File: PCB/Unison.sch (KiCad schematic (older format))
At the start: 262 parts, among them J1 USB4085-GF-A_REVA, J2 Conn_02x05_Odd_Even, J3 Conn_01x03, U1 ATmega32U4-AU, Y1 16MHz

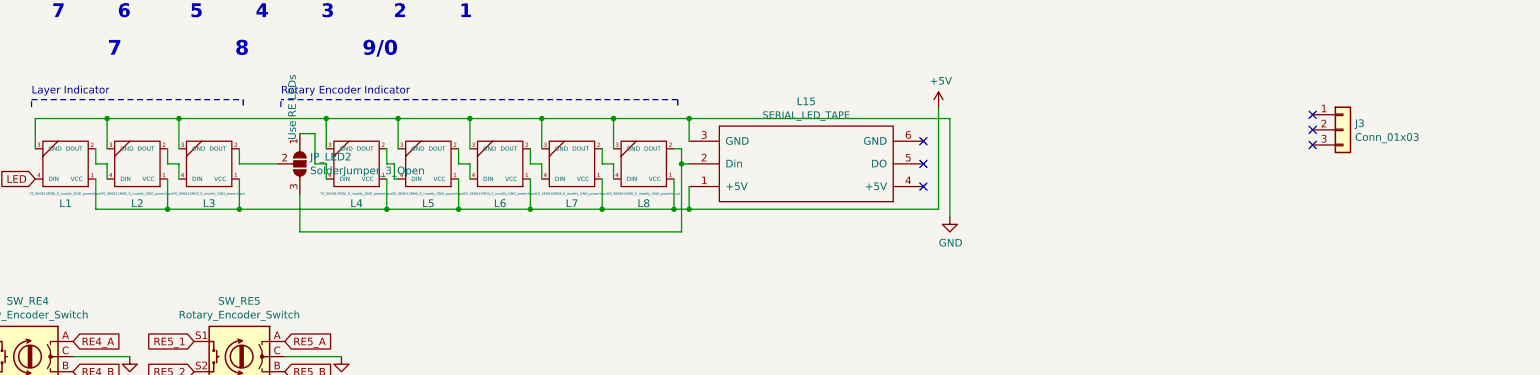
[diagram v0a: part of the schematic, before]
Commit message: OP-1スタイルで、4キー部分とミッドとトッププレートの間隔広げるに伴い、設置場所が狭くなるため、インジケータLEDを3個から2個に減らした。
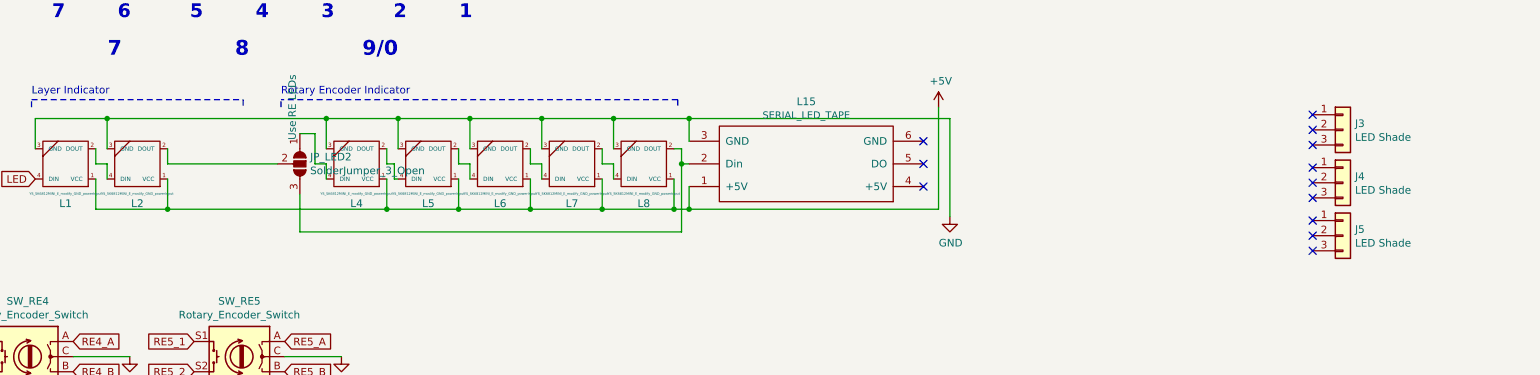
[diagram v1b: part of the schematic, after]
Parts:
- removed L3: YS_SK6812MINI_E_modify_GND_powerInput, mx2u:YS-SK6812MINI-E, symbol mx2u:YS_SK6812MINI_E_modify_GND_powerInput
- added J4, J5: LED Shade, Connector_PinSocket_2.54mm:PinSocket_1x03_P2.54mm_Vertical, symbol Connector_Generic:Conn_01x03
- J3: value Conn_01x03 -> LED Shade
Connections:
- net at JP_LED2.2 (C): now also L2.2 (DOUT)
- no-connect marks 9 -> 15
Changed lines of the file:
@@
 	6475 9525 6475 9625
-Wire Wire Line
-	6475 9625 6550 9625
-Wire Wire Line
-	6550 9625 6550 9725
-Wire Wire Line
-	6950 9525 6950 9625
 Wire Wire Line
 	7525 9625 7525 9725
@@
 	6475 9725 6475 9925
 Connection ~ 6475 9925
-Wire Wire Line
-	6475 9925 6950 9925
-Wire Wire Line
-	6950 9725 6950 9925
 Wire Wire Line
 	8400 9725 8400 9925
@@
 F 3 "" H 6275 9625 60  0001 C CNN
 	1    6275 9625
-	-1   0    0    1
-$EndComp
-$Comp
-L mx2u:YS_SK6812MINI_E_modify_GND_powerInput L3
-U 1 1 63211639
-P 6750 9625
-F 0 "L3" H 6750 9887 51  0000 C CNN
-F 1 "YS_SK6812MINI_E_modify_GND_powerInput" H 6750 9822 16  0000 C CNN
-F 2 "mx2u:YS-SK6812MINI-E" H 6750 9625 60  0001 C CNN
-F 3 "" H 6750 9625 60  0001 C CNN
-	1    6750 9625
 	-1   0    0    1
 $EndComp
@@
 Wire Wire Line
 	9425 9625 9425 9725
-Connection ~ 6950 9925
-Wire Wire Line
-	6950 9925 7925 9925
-Wire Wire Line
-	6950 9625 7200 9625
 Wire Wire Line
 	7350 9825 7350 10075
@@
 Wire Wire Line
 	6075 9325 5600 9325
-Wire Wire Line
-	6075 9325 6550 9325
 Connection ~ 6075 9325
 Wire Wire Line
 	6075 9525 6075 9325
-Wire Wire Line
-	6550 9525 6550 9325
-Wire Wire Line
-	6550 9325 7525 9325
-Connection ~ 6550 9325
 Connection ~ 7525 9325
 Wire Wire Line
@@
 P 14250 9400
 F 0 "J3" H 14330 9442 50  0000 L CNN
-F 1 "Conn_01x03" H 14330 9351 50  0000 L CNN
+F 1 "LED Shade" H 14330 9351 50  0000 L CNN
 F 2 "Connector_PinSocket_2.54mm:PinSocket_1x03_P2.54mm_Vertical" H 14250 9400 50  0001 C CNN
 F 3 "~" H 14250 9400 50  0001 C CNN
@@
 NoConn ~ 14050 9400
 NoConn ~ 14050 9500
+$Comp
+L Connector_Generic:Conn_01x03 J4
+U 1 1 60F74693
+P 14250 9750
+F 0 "J4" H 14330 9792 50  0000 L CNN
+F 1 "LED Shade" H 14330 9701 50  0000 L CNN
+F 2 "Connector_PinSocket_2.54mm:PinSocket_1x03_P2.54mm_Vertical" H 14250 9750 50  0001 C CNN
+F 3 "~" H 14250 9750 50  0001 C CNN
+	1    14250 9750
+	1    0    0    -1
+$EndComp
+NoConn ~ 14050 9650
+NoConn ~ 14050 9750
+NoConn ~ 14050 9850
+NoConn ~ 14050 10000
+NoConn ~ 14050 10100
+NoConn ~ 14050 10200
+$Comp
+L Connector_Generic:Conn_01x03 J5
+U 1 1 60FCE0DF
+P 14250 10100
+F 0 "J5" H 14330 10142 50  0000 L CNN
+F 1 "LED Shade" H 14330 10051 50  0000 L CNN
+F 2 "Connector_PinSocket_2.54mm:PinSocket_1x03_P2.54mm_Vertical" H 14250 10100 50  0001 C CNN
+F 3 "~" H 14250 10100 50  0001 C CNN
+	1    14250 10100
+	1    0    0    -1
+$EndComp
+Wire Wire Line
+	6075 9325 7525 9325
+Wire Wire Line
+	6475 9625 7200 9625
+Wire Wire Line
+	6475 9925 7925 9925
 $EndSCHEMATC

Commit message: Update: AU版、ひととおり完成。
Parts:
- removed J4, J5: LED Shade, Connector_PinSocket_2.54mm:PinSocket_1x03_P2.54mm_Vertical, symbol Connector_Generic:Conn_01x03
- removed L1, L2, L4, L5, L6, L7, L8: YS_SK6812MINI_E_modify_GND_powerInput, mx2u:YS-SK6812MINI-E, symbol mx2u:YS_SK6812MINI_E_modify_GND_powerInput
- added H1, H10, H11, H12, H13, H14, H15, H16, H17, H18, H2, H3, H4, H5, H6, H7, H8, H9: MountingHole, ukiha:M2_Hole, symbol Mechanical:MountingHole
- added J4: Conn_01x02, Connector_PinHeader_2.54mm:PinHeader_1x02_P2.54mm_Vertical, symbol Connector_Generic:Conn_01x02
- added JP_LED1: SolderJumper_3_Open, Jumper:SolderJumper-3_P1.3mm_Open_Pad1.0x1.5mm_NumberLabels, symbol Jumper:SolderJumper_3_Open
- added L1, L2, L3, L4, L5, L6, L7, L8, L9: SK6812MINI, LED_SMD:LED_SK6812MINI_PLCC4_3.5x3.5mm_P1.75mm, symbol swanmatch:SK6812MINI
- J2: value Conn_02x05_Odd_Even -> Conn_02x05[3_Odd_Even; footprint Connector_PinHeader_2.54mm:PinHeader_2x05_P2.54mm_Vertical -> Connector_PinHeader_2.54mm:PinHeader_2x03_P2.54mm_Vertical; symbol Connector_Generic:Conn_02x05_Odd_Even -> Connector_Generic:Conn_02x03_Odd_Even
- JP_LED2: Note Use RE LEDs -> RE LEDs
- SW_10_1, SW_12_1, SW_12_2, SW_13_1, SW_13_2, SW_14, SW_15, SW_16, SW_17_1, SW_19_1, SW_20_1, SW_23_1, SW_23_2, SW_24_1, SW_25_1, SW_26, SW_27_1, SW_27_2, SW_28_1, SW_28_2, SW_29, SW_30_1, SW_31, SW_32_1, SW_32_2, SW_34, SW_36_1, SW_36_2, SW_37_1, SW_38_1, SW_39_1, SW_40_1, SW_41_1, SW_41_2, SW_42, SW_43, SW_46_1, SW_46_2, SW_47, SW_48, SW_49, SW_50, SW_51_1, SW_51_2, SW_52, SW_54, SW_56, SW_57, SW_58, SW_59, SW_6, SW_60_1, SW_61, SW_62, SW_63, SW_64, SW_67, SW_68, SW_69, SW_70_1, SW_71, SW_72_1, SW_73_1, SW_74, SW_76, SW_78_1, SW_78_2, SW_79, SW_7_1, SW_80_1, SW_81, SW_82_1, SW_82_2, SW_83_1, SW_83_2, SW_84, SW_85_1, SW_86, SW_87_1, SW_87_2, SW_89, SW_9, SW_90_1, SW_94, SW_95, SW_96, SW_97_1, SW_97_2, SW_98_1, SW_98_2: footprint ukiha:CherryMX_MidHeight_16mm_rev2 -> ukiha:CherryMX_MidHeight_16mm_rev2_merged_hole
- SW_10_2, SW_19_2, SW_35_1, SW_35_2, SW_39_2, SW_45_1, SW_45_2, SW_65_1, SW_75_3, SW_85_2: footprint ukiha:CherryMX_MidHeight_16mm_rev2_2u_guide -> ukiha:CherryMX_MidHeight_16mm_rev2_merged_hole_2u_guide
- SW_17_2, SW_18_2, SW_20_2, SW_25_3, SW_30_2, SW_35_3, SW_38_2, SW_45_3, SW_45_4, SW_65_2, SW_65_3, SW_70_2, SW_72_2, SW_73_2, SW_7_2, SW_80_2, SW_85_3, SW_8_2: footprint ukiha:CherryMX_MidHeight_16mm_rev2_1.5u_guide -> ukiha:CherryMX_MidHeight_16mm_rev2_merged_hole_1.5u_guide
- SW_25_2, SW_60_2, SW_90_2: footprint ukiha:CherryMX_MidHeight_16mm_rev2_2U_vertical_guide -> ukiha:CherryMX_MidHeight_16mm_rev2_merged_hole_2U_vertical_guide
- SW_37_2: footprint ukiha:CherryMX_MidHeight_16mm_rev2_1.5u_alt_guide -> ukiha:CherryMX_MidHeight_16mm_rev2_merged_hole_1.5u_alt_guide
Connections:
- net +5V: now also L1.4 (VDD), L2.4 (VDD), L3.4 (VDD), L4.4 (VDD), L5.4 (VDD), L6.4 (VDD), L7.4 (VDD), L8.4 (VDD), L9.4 (VDD)
- net AUDIO: no longer J2.9 (Pin_9)
- net GND: now also L1.2 (VSS), L2.2 (VSS), L3.2 (VSS), L4.2 (VSS), L5.2 (VSS), L6.2 (VSS), L7.2 (VSS), L8.2 (VSS), L9.2 (VSS)
- net LED: now also L1.3 (DIN)
- net SCL: now also J4.2 (Pin_2); no longer J2.8 (Pin_8)
- net SDA: now also J4.1 (Pin_1); no longer J2.10 (Pin_10)
- net at JP_LED2.3 (B), L15.2 (Din): now also L9.1 (DOUT)
- net at JP_LED2.1 (A): now also L3.3 (DIN)
- net at JP_LED2.2 (C): now also L2.1 (DOUT)
- net Reserve: no longer names the net of U1.30 (PB6)
- net Reserve: no longer J2.7 (Pin_7)
- new net: JP_LED1.1 (A), L4.3 (DIN)
- new net: JP_LED1.2 (C), L3.1 (DOUT)
- new net: JP_LED1.3 (B), L5.1 (DOUT), L6.3 (DIN)
- new net: L1.1 (DOUT), L2.3 (DIN)
- new net: L4.1 (DOUT), L5.3 (DIN)
- new net: L6.1 (DOUT), L7.3 (DIN)
- new net: L7.1 (DOUT), L8.3 (DIN)
- new net: L8.1 (DOUT), L9.3 (DIN)
- no-connect marks 15 -> 10
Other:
- note added: "Optional LEDs"
- moved on the sheet: L15

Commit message: Update: MUに入れ替え。各部調整。
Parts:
- removed U1: ATmega32U4-AU, keebio:ATMEGA32U4-AU, symbol MCU_Microchip_ATmega:ATmega32U4-AU
- added U1: ATmega32U4-MU, swanmatch:QFN-44-1EP_7x7mm_Pitch0.5mm, symbol MCU_Microchip_ATmega:ATmega32U4-MU
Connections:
- net +5V: now also U1.14 (VCC), U1.2 (UVCC), U1.24 (AVCC), U1.34 (VCC), U1.44 (AVCC), U1.7 (VBUS)
- net AUDIO: now also U1.31 (PC6)
- net D+: now also U1.4 (D+)
- net D-: now also U1.3 (D-)
- net GND: now also U1.15 (GND), U1.23 (GND), U1.35 (GND), U1.43 (GND), U1.45 (GND), U1.5 (UGND)
- net LED: now also U1.12 (PB7)
- net RE1_A: now also U1.8 (PB0)
- net RE1_B: now also U1.9 (PB1)
- net RE2_A: now also U1.20 (PD2)
- net RE2_B: now also U1.21 (PD3)
- net RE3_A: now also U1.22 (PD5)
- net RE3_B: now also U1.25 (PD4)
- net RE4_A: now also U1.26 (PD6)
- net RE4_B: now also U1.27 (PD7)
- net RE5_A: now also U1.28 (PB4)
- net RE5_B: now also U1.29 (PB5)
- net RESET: now also U1.13 (~RESET)
- net SCL: now also U1.18 (PD0)
- net SDA: now also U1.19 (PD1)
- net pin1: now also U1.11 (PB3)
- net pin10: now also U1.32 (PC7)
- net pin2: now also U1.1 (PE6)
- net pin3: now also U1.40 (PF1)
- net pin4: now also U1.38 (PF5)
- net pin5: now also U1.36 (PF7)
- net pin6: now also U1.10 (PB2)
- net pin7: now also U1.41 (PF0)
- net pin8: now also U1.39 (PF4)
- net pin9: now also U1.37 (PF6)
- net at C6.1: now also U1.6 (UCAP)
- net at C2.1, Y1.1: now also U1.17 (XTAL1)
- net at C3.1, Y1.3: now also U1.16 (XTAL2)
- net at R9.2: now also U1.33 (~HWB~/PE2)
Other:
- note added: "Rotary Encoder LEDs"
- note removed: "Rotary Encoder Indicator"
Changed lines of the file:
@@
 	13250 4900 13500 4900
 $Comp
-L MCU_Microchip_ATmega:ATmega32U4-AU U1
-U 1 1 5D93C3AA
-P 14700 3625
-F 0 "U1" H 14700 1739 50  0000 C CNN
-F 1 "ATmega32U4-AU" H 14700 1648 50  0000 C CNN
-F 2 "keebio:ATMEGA32U4-AU" H 14700 3625 50  0001 C CIN
-F 3 "http://ww1.microchip.com/downloads/en/DeviceDoc/Atmel-7766-8-bit-AVR-ATmega16U4-32U4_Datasheet.pdf" H 14700 3625 50  0001 C CNN
-F 4 "C45874" H 14700 3625 50  0001 C CNN "LCSC"
-	1    14700 3625
-	1    0    0    -1
-$EndComp
-$Comp
 L power:+5V #PWR030
 U 1 1 5D9BA68C
@@
 Wire Notes Line
 	11425 9100 11425 9150
-Text Notes 7225 9075 0    50   ~ 0
-Rotary Encoder Indicator
 NoConn ~ 13050 9625
 Wire Wire Line
@@
 Wire Wire Line
 	7475 9925 8350 9925
+$Comp
+L MCU_Microchip_ATmega:ATmega32U4-MU U1
+U 1 1 601BC257
+P 14700 3625
+F 0 "U1" H 14700 1736 50  0000 C CNN
+F 1 "ATmega32U4-MU" H 14700 1645 50  0000 C CNN
+F 2 "swanmatch:QFN-44-1EP_7x7mm_Pitch0.5mm" H 14700 3625 50  0001 C CIN
+F 3 "http://ww1.microchip.com/downloads/en/DeviceDoc/Atmel-7766-8-bit-AVR-ATmega16U4-32U4_Datasheet.pdf" H 14700 3625 50  0001 C CNN
+	1    14700 3625
+	1    0    0    -1
+$EndComp
+Text Notes 7225 9075 0    50   ~ 0
+Rotary Encoder LEDs
 $EndSCHEMATC

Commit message: Update: 発注用データ準備。F1, D102はSMTに含めない。
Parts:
- U1: LCSC (none) -> C45874
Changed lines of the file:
@@
 F 2 "swanmatch:QFN-44-1EP_7x7mm_Pitch0.5mm" H 14700 3625 50  0001 C CIN
 F 3 "http://ww1.microchip.com/downloads/en/DeviceDoc/Atmel-7766-8-bit-AVR-ATmega16U4-32U4_Datasheet.pdf" H 14700 3625 50  0001 C CNN
+F 4 "C45874" H 14700 3625 50  0001 C CNN "LCSC"
 	1    14700 3625
 	1    0    0    -1

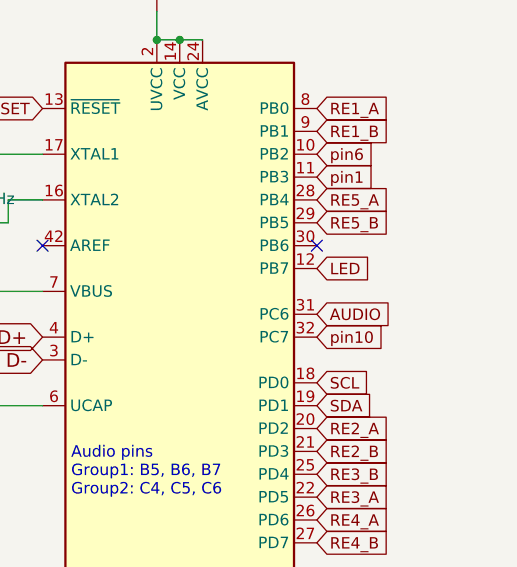
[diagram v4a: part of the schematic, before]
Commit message: ピンB6を2本目のオーディオピンとして接続。
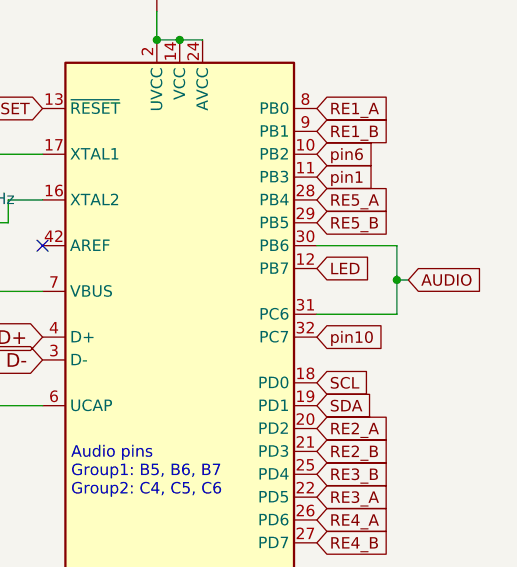
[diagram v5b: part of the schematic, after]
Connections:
- net AUDIO: now also U1.30 (PB6)
- no-connect marks 10 -> 9
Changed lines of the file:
@@
 	-1   0    0    1
 $EndComp
-Text GLabel 1450 9925 2    50   Input ~ 0
-AUDIO
 $Comp
 L power:GND #PWR01
@@
 Wire Wire Line
 	925  10025 925  10225
-Text GLabel 15300 3025 2    50   Input ~ 0
-AUDIO
 Connection ~ 4800 6575
 Wire Wire Line
@@
 Text Notes 8100 9225 0    50   ~ 0
 Optional LEDs
-NoConn ~ 15300 2725
 $Comp
 L Connector_Generic:Conn_01x02 J4
@@
 Text Notes 7225 9075 0    50   ~ 0
 Rotary Encoder LEDs
+Text GLabel 1450 9925 2    50   Input ~ 0
+AUDIO
+Text GLabel 15700 2875 2    50   Input ~ 0
+AUDIO
+Wire Wire Line
+	15300 2725 15650 2725
+Wire Wire Line
+	15650 2725 15650 2875
+Wire Wire Line
+	15650 3025 15300 3025
+Wire Wire Line
+	15650 2875 15700 2875
+Connection ~ 15650 2875
+Wire Wire Line
+	15650 2875 15650 3025
 $EndSCHEMATC

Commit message: 中央下をネジ止めせずに使用するため、スイッチのフットプリントを非ソケットに変更。
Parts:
- SW_60_3, SW_75_1: footprint ukiha:MXOnly-2U-NoLED_16mm -> ukiha:CherryMX_MidHeight_16mm_rev2_merged_hole_2u_guide
- SW_75_2: footprint ukiha:MXOnly-1.5U-NoLED_16mm -> ukiha:CherryMX_MidHeight_16mm_rev2_merged_hole_1.5u_guide
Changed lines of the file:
@@
 F 0 "SW_75_1" H 8250 8110 50  0000 C CNN
 F 1 "SW_Push" H 8250 8019 50  0000 C CNN
-F 2 "ukiha:MXOnly-2U-NoLED_16mm" H 8250 8025 50  0001 C CNN
+F 2 "ukiha:CherryMX_MidHeight_16mm_rev2_merged_hole_2u_guide" H 8250 8025 50  0001 C CNN
 F 3 "~" H 8250 8025 50  0001 C CNN
 	1    8250 7825
@@
 F 0 "SW_75_2" H 8250 7935 50  0000 C CNN
 F 1 "SW_Push" H 8250 7844 50  0000 C CNN
-F 2 "ukiha:MXOnly-1.5U-NoLED_16mm" H 8250 7850 50  0001 C CNN
+F 2 "ukiha:CherryMX_MidHeight_16mm_rev2_merged_hole_1.5u_guide" H 8250 7850 50  0001 C CNN
 F 3 "~" H 8250 7850 50  0001 C CNN
 	1    8250 7650
@@
 F 0 "SW_60_3" H 7600 7760 50  0000 C CNN
 F 1 "SW_Push" H 7600 7669 50  0000 C CNN
-F 2 "ukiha:MXOnly-2U-NoLED_16mm" H 7600 7675 50  0001 C CNN
+F 2 "ukiha:CherryMX_MidHeight_16mm_rev2_merged_hole_2u_guide" H 7600 7675 50  0001 C CNN
 F 3 "~" H 7600 7675 50  0001 C CNN
 	1    7600 7475

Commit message: スイッチをガッチリと固定できるフットプリントに変更。配線調整。
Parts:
- SW_10_1, SW_12_1, SW_12_2, SW_13_1, SW_13_2, SW_14, SW_15, SW_16, SW_17_1, SW_19_1, SW_20_1, SW_23_1, SW_23_2, SW_24_1, SW_25_1, SW_26, SW_27_1, SW_27_2, SW_28_1, SW_28_2, SW_29, SW_30_1, SW_31, SW_32_1, SW_32_2, SW_34, SW_36_1, SW_36_2, SW_37_1, SW_38_1, SW_39_1, SW_40_1, SW_41_1, SW_41_2, SW_42, SW_43, SW_46_1, SW_46_2, SW_47, SW_48, SW_49, SW_50, SW_51_1, SW_51_2, SW_52, SW_54, SW_56, SW_57, SW_58, SW_59, SW_6, SW_60_1, SW_61, SW_62, SW_63, SW_64, SW_67, SW_68, SW_69, SW_70_1, SW_71, SW_72_1, SW_73_1, SW_74, SW_76, SW_78_1, SW_78_2, SW_79, SW_7_1, SW_80_1, SW_81, SW_82_1, SW_82_2, SW_83_1, SW_83_2, SW_84, SW_85_1, SW_86, SW_87_1, SW_87_2, SW_89, SW_9, SW_90_1, SW_94, SW_95, SW_96, SW_97_1, SW_97_2, SW_98_1, SW_98_2: footprint ukiha:CherryMX_MidHeight_16mm_rev2_merged_hole -> ukiha:CherryMX_MidHeight_16mm_rev2
- SW_10_2, SW_19_2, SW_35_1, SW_35_2, SW_39_2, SW_45_1, SW_45_2, SW_60_3, SW_65_1, SW_75_1, SW_75_3, SW_85_2: footprint ukiha:CherryMX_MidHeight_16mm_rev2_merged_hole_2u_guide -> ukiha:CherryMX_MidHeight_16mm_rev2_2u_guide
- SW_17_2, SW_18_2, SW_20_2, SW_25_3, SW_30_2, SW_35_3, SW_38_2, SW_45_3, SW_45_4, SW_65_2, SW_65_3, SW_70_2, SW_72_2, SW_73_2, SW_75_2, SW_7_2, SW_80_2, SW_85_3, SW_8_2: footprint ukiha:CherryMX_MidHeight_16mm_rev2_merged_hole_1.5u_guide -> ukiha:CherryMX_MidHeight_16mm_rev2_1.5u_guide
- SW_25_2, SW_60_2, SW_90_2: footprint ukiha:CherryMX_MidHeight_16mm_rev2_merged_hole_2U_vertical_guide -> ukiha:CherryMX_MidHeight_16mm_rev2_2U_vertical_guide
- SW_37_2: footprint ukiha:CherryMX_MidHeight_16mm_rev2_merged_hole_1.5u_alt_guide -> ukiha:CherryMX_MidHeight_16mm_rev2_1.5u_alt_guide

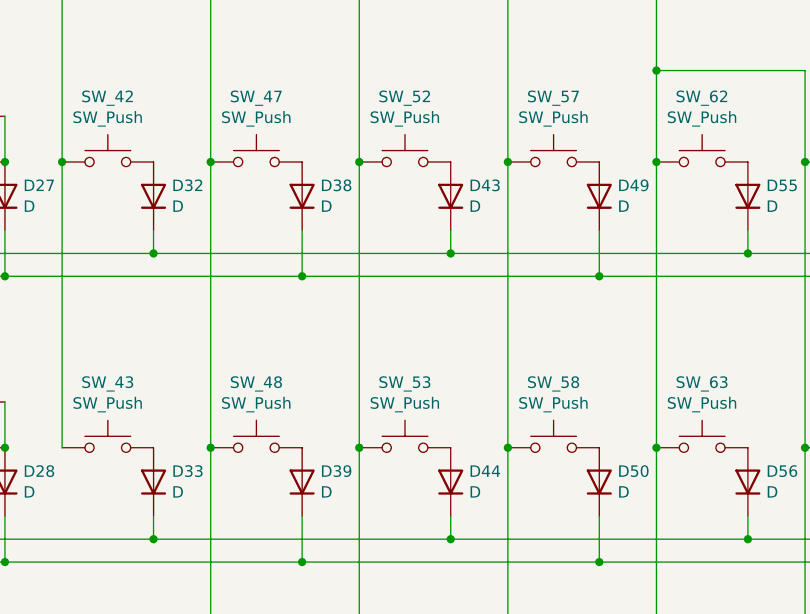
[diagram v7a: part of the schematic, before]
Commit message: ネジ穴にかぶるスイッチをKailhソケット化
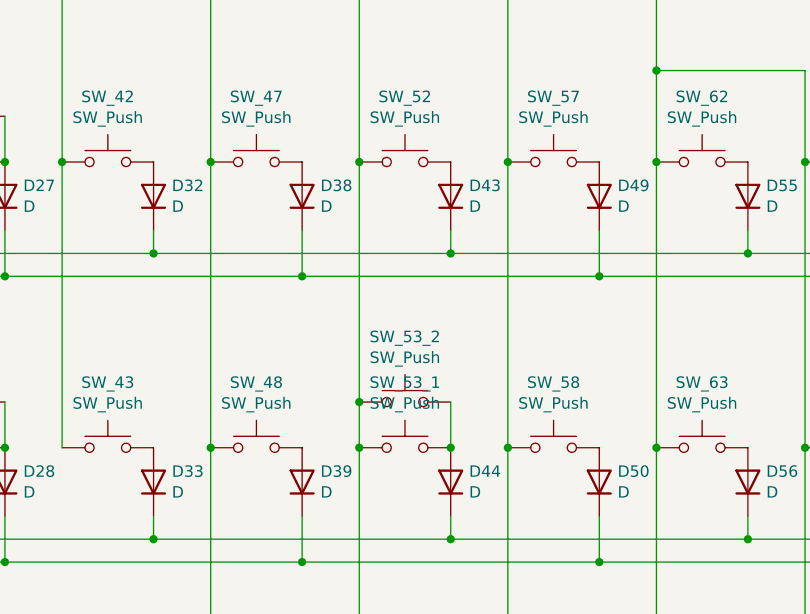
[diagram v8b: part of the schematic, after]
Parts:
- added SW_53_2: SW_Push, ukiha:MXOnly-1U-Hotswap_16mm_guide, symbol Switch:SW_Push
- SW_18_1, SW_21, SW_8_1, SW_91: footprint ukiha:MXOnly-1U-NoLED_16mm -> ukiha:MXOnly-1U-Hotswap_16mm_guide
- SW_53_1: renamed from SW_53; footprint ukiha:MXOnly-1U-NoLED_16mm -> ukiha:CherryMX_MidHeight_16mm_rev2
- SW_8_2: footprint ukiha:CherryMX_MidHeight_16mm_rev2_1.5u_guide -> ukiha:CherryMX_MidHeight_16mm_rev2_1.5u_alt_guide
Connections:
- net at D47.1 (K), SW_50.1, SW_51_1.1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: now also SW_53_2.1
- net at D44.2 (A), SW_53_1.2: now also SW_53_2.2
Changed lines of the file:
@@
 F 0 "SW_21" H 1750 3110 50  0000 C CNN
 F 1 "SW_Push" H 1750 3019 50  0000 C CNN
-F 2 "ukiha:MXOnly-1U-NoLED_16mm" H 1750 3025 50  0001 C CNN
+F 2 "ukiha:MXOnly-1U-Hotswap_16mm_guide" H 1750 3025 50  0001 C CNN
 F 3 "~" H 1750 3025 50  0001 C CNN
 	1    1750 2825
@@
 F 0 "SW_18_1" H 1100 5610 50  0000 C CNN
 F 1 "SW_Push" H 1100 5519 50  0000 C CNN
-F 2 "ukiha:MXOnly-1U-NoLED_16mm" H 1100 5525 50  0001 C CNN
+F 2 "ukiha:MXOnly-1U-Hotswap_16mm_guide" H 1100 5525 50  0001 C CNN
 F 3 "~" H 1100 5525 50  0001 C CNN
 	1    1100 5325
@@
 $EndComp
 $Comp
-L Switch:SW_Push SW_53
+L Switch:SW_Push SW_53_1
 U 1 1 5F6658AB
 P 5650 5325
-F 0 "SW_53" H 5650 5610 50  0000 C CNN
+F 0 "SW_53_1" H 5650 5610 50  0000 C CNN
 F 1 "SW_Push" H 5650 5519 50  0000 C CNN
-F 2 "ukiha:MXOnly-1U-NoLED_16mm" H 5650 5525 50  0001 C CNN
+F 2 "ukiha:CherryMX_MidHeight_16mm_rev2" H 5650 5525 50  0001 C CNN
 F 3 "~" H 5650 5525 50  0001 C CNN
 	1    5650 5325
@@
 F 0 "SW_91" H 10850 3110 50  0000 C CNN
 F 1 "SW_Push" H 10850 3019 50  0000 C CNN
-F 2 "ukiha:MXOnly-1U-NoLED_16mm" H 10850 3025 50  0001 C CNN
+F 2 "ukiha:MXOnly-1U-Hotswap_16mm_guide" H 10850 3025 50  0001 C CNN
 F 3 "~" H 10850 3025 50  0001 C CNN
 	1    10850 2825
@@
 F 0 "SW_8_1" H 11500 5610 50  0000 C CNN
 F 1 "SW_Push" H 11500 5519 50  0000 C CNN
-F 2 "ukiha:MXOnly-1U-NoLED_16mm" H 11500 5525 50  0001 C CNN
+F 2 "ukiha:MXOnly-1U-Hotswap_16mm_guide" H 11500 5525 50  0001 C CNN
 F 3 "~" H 11500 5525 50  0001 C CNN
 F 4 "SW_08" H 11500 5900 50  0000 C CNN "Alt Ref"
@@
 $EndComp
 Wire Wire Line
-	5450 4075 5450 5325
+	5450 4075 5450 5125
 Wire Wire Line
 	775  4475 1950 4475
@@
 F 0 "SW_8_2" H 11500 5410 50  0000 C CNN
 F 1 "SW_Push" H 11500 5319 50  0000 C CNN
-F 2 "ukiha:CherryMX_MidHeight_16mm_rev2_1.5u_guide" H 11500 5325 50  0001 C CNN
+F 2 "ukiha:CherryMX_MidHeight_16mm_rev2_1.5u_alt_guide" H 11500 5325 50  0001 C CNN
 F 3 "~" H 11500 5325 50  0001 C CNN
 	1    11500 5125
@@
 Wire Wire Line
 	15650 2875 15650 3025
+$Comp
+L Switch:SW_Push SW_53_2
+U 1 1 604D573F
+P 5650 5125
+F 0 "SW_53_2" H 5650 5410 50  0000 C CNN
+F 1 "SW_Push" H 5650 5319 50  0000 C CNN
+F 2 "ukiha:MXOnly-1U-Hotswap_16mm_guide" H 5650 5325 50  0001 C CNN
+F 3 "~" H 5650 5325 50  0001 C CNN
+	1    5650 5125
+	1    0    0    -1
+$EndComp
+Connection ~ 5450 5125
+Wire Wire Line
+	5450 5125 5450 5325
+Wire Wire Line
+	5850 5125 5850 5325
+Connection ~ 5850 5325
 $EndSCHEMATC
